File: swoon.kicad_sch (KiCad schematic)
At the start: 130 parts, among them J1 3305-0-15-80-47-27-10-0, J10 3305-0-15-80-47-27-10-0, J11 3305-0-15-80-47-27-10-0, J12 3305-0-15-80-47-27-10-0, J13 3305-0-15-80-47-27-10-0, J14 3305-0-15-80-47-27-10-0, J15 3305-0-15-80-47-27-10-0, J16 3305-0-15-80-47-27-10-0, J17 3305-0-15-80-47-27-10-0, J18 3305-0-15-80-47-27-10-0, J19 3305-0-15-80-47-27-10-0, J2 3305-0-15-80-47-27-10-0, J20 3305-0-15-80-47-27-10-0, J21 3305-0-15-80-47-27-10-0, J22 3305-0-15-80-47-27-10-0, J23 3305-0-15-80-47-27-10-0, J24 3305-0-15-80-47-27-10-0, J25 3305-0-15-80-47-27-10-0, J26 3305-0-15-80-47-27-10-0, J27 3305-0-15-80-47-27-10-0, J28 3305-0-15-80-47-27-10-0, J29 3305-0-15-80-47-27-10-0, J3 3305-0-15-80-47-27-10-0, J30 3305-0-15-80-47-27-10-0, J31 3305-0-15-80-47-27-10-0, J32 3305-0-15-80-47-27-10-0, J33 3305-0-15-80-47-27-10-0, J34 3305-0-15-80-47-27-10-0, J35 3305-0-15-80-47-27-10-0, J36 3305-0-15-80-47-27-10-0, J37 3305-0-15-80-47-27-10-0, J38 3305-0-15-80-47-27-10-0, J39 3305-0-15-80-47-27-10-0, J4 3305-0-15-80-47-27-10-0, J40 3305-0-15-80-47-27-10-0, J41 3305-0-15-80-47-27-10-0, J42 3305-0-15-80-47-27-10-0, J43 3305-0-15-80-47-27-10-0, J44 3305-0-15-80-47-27-10-0, J45 3305-0-15-80-47-27-10-0, J46 3305-0-15-80-47-27-10-0, J47 3305-0-15-80-47-27-10-0, J48 3305-0-15-80-47-27-10-0, J49 3305-0-15-80-47-27-10-0, J5 3305-0-15-80-47-27-10-0, J50 3305-0-15-80-47-27-10-0, J51 3305-0-15-80-47-27-10-0, J52 3305-0-15-80-47-27-10-0, J53 3305-0-15-80-47-27-10-0, J54 3305-0-15-80-47-27-10-0, J55 3305-0-15-80-47-27-10-0, J56 3305-0-15-80-47-27-10-0, J57 3305-0-15-80-47-27-10-0, J58 3305-0-15-80-47-27-10-0, J59 3305-0-15-80-47-27-10-0, J6 3305-0-15-80-47-27-10-0, J60 3305-0-15-80-47-27-10-0, J61 3305-0-15-80-47-27-10-0, J62 3305-0-15-80-47-27-10-0, J63 3305-0-15-80-47-27-10-0, J64 3305-0-15-80-47-27-10-0, J65 3305-0-15-80-47-27-10-0, J66 3305-0-15-80-47-27-10-0, J67 3305-0-15-80-47-27-10-0, J68 3305-0-15-80-47-27-10-0, J69 MF254V-11-07-0743, J7 3305-0-15-80-47-27-10-0, J70 MF254V-11-07-0743, J71 MF254V-11-07-0743, J72 MF254V-11-07-0743, J73 Mill Max 0906-2-15-20-75-14-1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, J74 Mill Max 0906-2-15-20-75-14-1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, J75 JST SM02B-SRSS-TB(LF)(SN), J76 JST SM02B-SRSS-TB(LF)(SN), J8 3305-0-15-80-47-27-10-0, J9 3305-0-15-80-47-27-10-0, SW1 SW_Push, SW10 SW_Push, SW11 SW_Push, SW12 SW_Push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

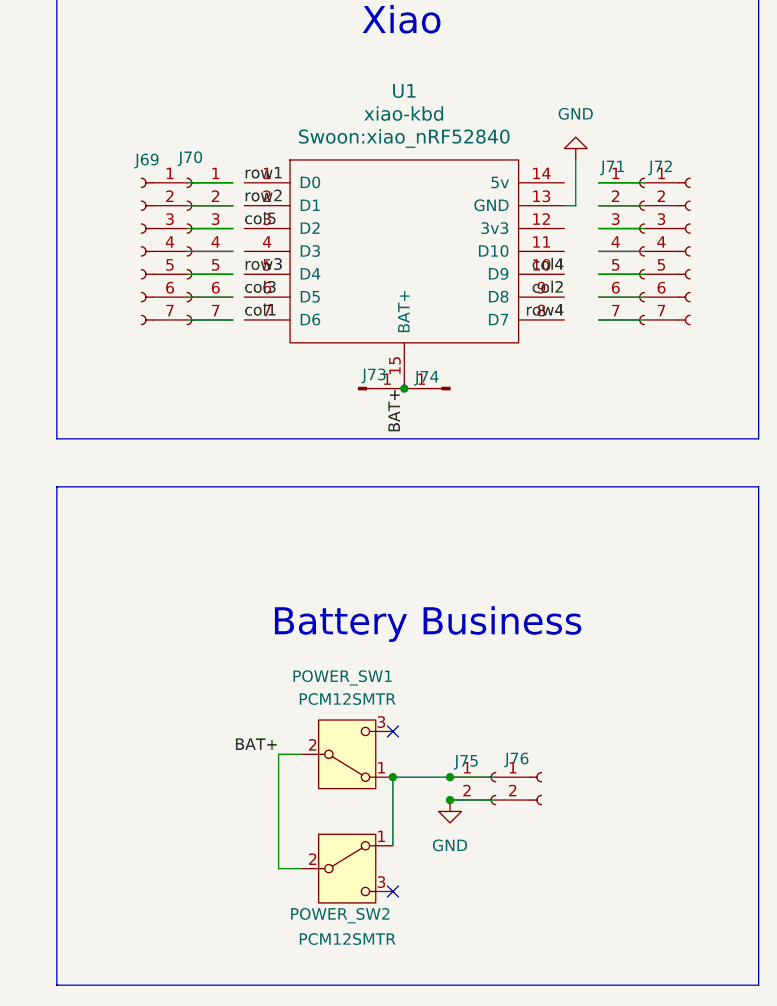
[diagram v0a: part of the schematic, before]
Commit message: position battery terminal & power switch
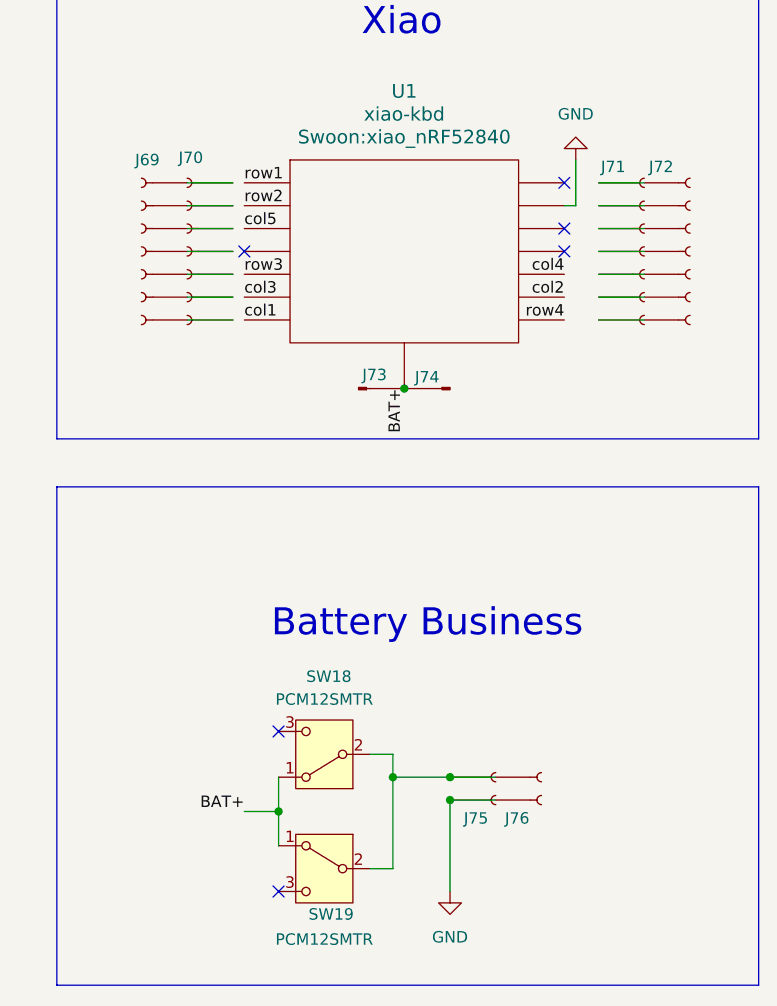
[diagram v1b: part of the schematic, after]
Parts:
- renumbered POWER_SW1 to SW18, POWER_SW2 to SW19
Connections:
- net BAT+: now also SW18.1 (A), SW19.1 (A); no longer SW18.2 (B), SW19.2 (B)
- net GND: now also J75.1 (Pin_1), J76.1 (Pin_1); no longer J75.2 (Pin_2), J76.2 (Pin_2)
- new net: J75.2 (Pin_2), J76.2 (Pin_2), SW18.2 (B), SW19.2 (B)
- no-connect marks 2 -> 6
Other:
- moved on the sheet: SW18, SW19

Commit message: add tenting puck, copper graphic
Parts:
- added H1: Puck_Mounting_Pad, Swoon:Tenting_Puck2, symbol Mechanical:MountingHole_Pad_MP
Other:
- note added: "Mounting Puck"
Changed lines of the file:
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@@
 	)
 	(rectangle
+		(start 24.892 166.37)
+		(end 172.466 192.278)
+		(stroke
+			(width 0)
+			(type default)
+		)
+		(fill
+			(type none)
+		)
+	)
+	(rectangle
 		(start 186.182 32.766)
 		(end 264.16 88.138)
@@
 		)
 	)
+	(text "Mounting Puck\n"
+		(exclude_from_sim no)
+		(at 70.612 178.816 0)
+		(effects
+			(font
+				(size 2.9972 2.9972)
+			)
+		)
+	)
 	(text "Battery Business"
 		(exclude_from_sim no)
@@
 					(unit 1)
 				)
+			)
+		)
+	)
+	(symbol
+		(lib_id "Mechanical:MountingHole_Pad_MP")
+		(at 104.14 179.07 0)
+		(unit 1)
+		(exclude_from_sim yes)
+		(in_bom no)
+		(on_board yes)
+		(dnp no)
+		(fields_autoplaced yes)
+		(property "Reference" "H1"
+			(at 106.68 176.5299 0)
+			(effects
+				(font
+					(size 1.27 1.27)
+				)
+				(justify left)
+			)
+		)
+		(property "Value" "Puck_Mounting_Pad"
+			(at 106.68 179.0699 0)
+			(effects
+				(font
+					(size 1.27 1.27)
+				)
+				(justify left)
+			)
+		)
+		(property "Footprint" "Swoon:Tenting_Puck2"
+			(at 104.14 179.07 0)
+			(effects
+				(font
+					(size 1.27 1.27)
+				)
+				(hide yes)
+			)
+		)
+		(property "Datasheet" "~"
+			(at 104.14 179.07 0)
+			(effects
+				(font
+					(size 1.27 1.27)
+				)
+				(hide yes)
+			)
+		)
+		(property "Description" "Mounting Hole with connection as pad named MP"
+			(at 104.14 179.07 0)
+			(effects
+				(font
+					(size 1.27 1.27)
+				)
+				(hide yes)
+			)
+		)
+		(pin "MP"
+		)
+		(instances
+			(project ""
+				(path "/1418ad6a-8a4d-429d-b07e-469b1ffa21a0"
+					(reference "H1")
+					(unit 1)
+				)

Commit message: add kicad action
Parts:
- D1, D10, D11, D12, D13, D14, D15, D16, D17, D18, D19, D2, D20, D21, D22, D23, D24, D25, D26, D27, D28, D29, D3, D30, D31, D32, D33, D34, D4, D5, D6, D7, D8, D9: footprint Diode_SMD:D_0805_2012Metric -> Swoon:D_0805_2012Metric
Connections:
- no-connect marks 6 -> 7
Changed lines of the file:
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@@
 	)
 	(no_connect
+		(at 104.14 181.61)
+	)
+	(no_connect
 		(at 210.82 120.65)
 	)
@@
 			)
 		)
-		(property "Footprint" "Diode_SMD:D_0805_2012Metric"
+		(property "Footprint" "Swoon:D_0805_2012Metric"
 			(at 142.24 82.55 0)
 			(effects
@@
 			)
 		)
-		(property "Footprint" "Diode_SMD:D_0805_2012Metric"
+		(property "Footprint" "Swoon:D_0805_2012Metric"
 			(at 77.47 123.19 0)
 			(effects
@@
 			)
 		)
-		(property "Footprint" "Diode_SMD:D_0805_2012Metric"
+		(property "Footprint" "Swoon:D_0805_2012Metric"
 			(at 97.79 82.55 0)
 			(effects
@@
 			)
 		)
-		(property "Footprint" "Diode_SMD:D_0805_2012Metric"
+		(property "Footprint" "Swoon:D_0805_2012Metric"
 			(at 142.24 102.87 0)
 			(effects
@@
 			)
 		)
-		(property "Footprint" "Diode_SMD:D_0805_2012Metric"
+		(property "Footprint" "Swoon:D_0805_2012Metric"
 			(at 57.15 62.23 0)
 			(effects
@@
 			)
 		)
-		(property "Footprint" "Diode_SMD:D_0805_2012Metric"
+		(property "Footprint" "Swoon:D_0805_2012Metric"
 			(at 81.28 102.87 0)
 			(effects
@@
 			)
 		)
-		(property "Footprint" "Diode_SMD:D_0805_2012Metric"
+		(property "Footprint" "Swoon:D_0805_2012Metric"
 			(at 60.96 123.19 0)
 			(effects
@@
 			)
 		)
-		(property "Footprint" "Diode_SMD:D_0805_2012Metric"
+		(property "Footprint" "Swoon:D_0805_2012Metric"
 			(at 97.79 62.23 0)
 			(effects
@@
 			)
 		)
-		(property "Footprint" "Diode_SMD:D_0805_2012Metric"
+		(property "Footprint" "Swoon:D_0805_2012Metric"
 			(at 81.28 123.19 0)
 			(effects
@@
 			)
 		)
-		(property "Footprint" "Diode_SMD:D_0805_2012Metric"
+		(property "Footprint" "Swoon:D_0805_2012Metric"
 			(at 77.47 82.55 0)
 			(effects
@@
 			)
 		)
-		(property "Footprint" "Diode_SMD:D_0805_2012Metric"
+		(property "Footprint" "Swoon:D_0805_2012Metric"
 			(at 60.96 62.23 0)
 			(effects
@@
 			)
 		)
-		(property "Footprint" "Diode_SMD:D_0805_2012Metric"
+		(property "Footprint" "Swoon:D_0805_2012Metric"
 			(at 77.47 62.23 0)
 			(effects
@@
 			)
 		)
-		(property "Footprint" "Diode_SMD:D_0805_2012Metric"
+		(property "Footprint" "Swoon:D_0805_2012Metric"
 			(at 57.15 102.87 0)
 			(effects
@@
 			)
 		)
+		(property "LCSC" ""
+			(at 224.79 67.31 0)
+			(effects
+				(font
+					(size 1.27 1.27)
+				)
+				(hide yes)
+			)
+		)
 		(pin "11"
 		)
@@
 			)
 		)
-		(property "Footprint" "Diode_SMD:D_0805_2012Metric"
+		(property "Footprint" "Swoon:D_0805_2012Metric"
 			(at 101.6 82.55 0)
 			(effects
@@
 			)
 		)
-		(property "Footprint" "Diode_SMD:D_0805_2012Metric"
+		(property "Footprint" "Swoon:D_0805_2012Metric"
 			(at 138.43 62.23 0)
 			(effects
@@
 			)
 		)
-		(property "Footprint" "Diode_SMD:D_0805_2012Metric"
+		(property "Footprint" "Swoon:D_0805_2012Metric"
 			(at 101.6 62.23 0)
 			(effects
@@
 			)
 		)
-		(property "Footprint" "Diode_SMD:D_0805_2012Metric"
+		(property "Footprint" "Swoon:D_0805_2012Metric"
 			(at 121.92 82.55 0)
 			(effects
@@
 			)
 		)
-		(property "Footprint" "Diode_SMD:D_0805_2012Metric"
+		(property "Footprint" "Swoon:D_0805_2012Metric"
 			(at 60.96 102.87 0)
 			(effects
@@
 			)
 		)
-		(property "Footprint" "Diode_SMD:D_0805_2012Metric"
+		(property "Footprint" "Swoon:D_0805_2012Metric"
 			(at 121.92 62.23 0)
 			(effects
@@
 			)
 		)
-		(property "Footprint" "Diode_SMD:D_0805_2012Metric"
+		(property "Footprint" "Swoon:D_0805_2012Metric"
 			(at 101.6 102.87 0)
 			(effects
@@
 			)
 		)
-		(property "Footprint" "Diode_SMD:D_0805_2012Metric"
+		(property "Footprint" "Swoon:D_0805_2012Metric"
 			(at 118.11 62.23 0)
 			(effects
@@
 			)
 		)
-		(property "Footprint" "Diode_SMD:D_0805_2012Metric"
+		(property "Footprint" "Swoon:D_0805_2012Metric"
 			(at 60.96 82.55 0)
 			(effects
@@
 			)
 		)
-		(property "Footprint" "Diode_SMD:D_0805_2012Metric"
+		(property "Footprint" "Swoon:D_0805_2012Metric"
 			(at 77.47 102.87 0)
 			(effects
@@
 			)
 		)
-		(property "Footprint" "Diode_SMD:D_0805_2012Metric"
+		(property "Footprint" "Swoon:D_0805_2012Metric"
 			(at 81.28 82.55 0)
 			(effects
@@
 			)
 		)
-		(property "Footprint" "Diode_SMD:D_0805_2012Metric"
+		(property "Footprint" "Swoon:D_0805_2012Metric"
 			(at 81.28 62.23 0)
 			(effects
@@
 			)
 		)
-		(property "Footprint" "Diode_SMD:D_0805_2012Metric"
+		(property "Footprint" "Swoon:D_0805_2012Metric"
 			(at 57.15 123.19 0)
 			(effects
@@
 			)
 		)
-		(property "Footprint" "Diode_SMD:D_0805_2012Metric"
+		(property "Footprint" "Swoon:D_0805_2012Metric"
 			(at 57.15 82.55 0)
 			(effects
@@
 			)
 		)
-		(property "Footprint" "Diode_SMD:D_0805_2012Metric"
+		(property "Footprint" "Swoon:D_0805_2012Metric"
 			(at 138.43 82.55 0)
 			(effects
@@
 			)
 		)
-		(property "Footprint" "Diode_SMD:D_0805_2012Metric"
+		(property "Footprint" "Swoon:D_0805_2012Metric"
 			(at 97.79 102.87 0)
 			(effects
@@
 			)
 		)
-		(property "Footprint" "Diode_SMD:D_0805_2012Metric"
+		(property "Footprint" "Swoon:D_0805_2012Metric"
 			(at 118.11 102.87 0)
 			(effects
@@
 			)
 		)
-		(property "Footprint" "Diode_SMD:D_0805_2012Metric"
+		(property "Footprint" "Swoon:D_0805_2012Metric"
 			(at 121.92 102.87 0)
 			(effects
@@
 			)
 		)
-		(property "Footprint" "Diode_SMD:D_0805_2012Metric"
+		(property "Footprint" "Swoon:D_0805_2012Metric"
 			(at 142.24 62.23 0)
 			(effects
@@
 			)
 		)
-		(property "Footprint" "Diode_SMD:D_0805_2012Metric"
+		(property "Footprint" "Swoon:D_0805_2012Metric"
 			(at 118.11 82.55 0)
 			(effects
@@
 			)
 		)
-		(property "Footprint" "Diode_SMD:D_0805_2012Metric"
+		(property "Footprint" "Swoon:D_0805_2012Metric"
 			(at 138.43 102.87 0)
 			(effects

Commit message: add kibot file
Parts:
- removed J75, J76: JST SM02B-SRSS-TB(LF)(SN), Swoon:JST_SH_SM02B-SRSS-TB_1x02-1MP_P1.00mm_Horizontal, symbol Connector:Conn_01x02_Socket
- removed SW18, SW19: PCM12SMTR, Swoon:SW_PCM12SMTR, symbol Switch:SW_SPDT
- added SW18, SW19: MST22D18G2 125, Swoon:SW-SMD_MST22D18G2, symbol Swoon:MST22D18G2125
- added U2, U3: MY-LR44-02, Swoon:BAT-SMD_MY-LR44-02, symbol Swoon:MY-LR44-02
- D1, D10, D11, D12, D13, D14, D15, D16, D17, D18, D19, D2, D20, D21, D22, D23, D24, D25, D26, D27, D28, D29, D3, D30, D31, D32, D33, D34, D4, D5, D6, D7, D8, D9: value CD4148WSP-C109001 -> CD4148W; footprint Swoon:D_0805_2012Metric -> Diode_SMD:D_0805_2012Metric; LCSC (none) -> C109001
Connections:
- net BAT+: now also SW18.1, SW18.2, SW18.4, SW18.5, SW19.1, SW19.2, SW19.4, SW19.5
- net GND: now also U2.2, U3.2
- new net: SW18.3, SW18.6, SW19.3, SW19.6, U2.1, U3.1
- no-connect marks 7 -> 5

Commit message: add variants
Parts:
- added TP1, TP10, TP11, TP12, TP13, TP14, TP15, TP16, TP17, TP18, TP19, TP2, TP20, TP3, TP4, TP5, TP6, TP7, TP8, TP9: TestPoint_Small, TestPoint:TestPoint_Pad_1.0x1.0mm, symbol Connector:TestPoint_Small
- D1, D11, D13, D15, D17, D19, D21, D23, D25, D27, D29, D3, D31, D33, D5, D7, D9: value CD4148W -> CD4148WS; footprint Diode_SMD:D_0805_2012Metric -> Swoon:D_0805_2012Metric; Config (none) -> +left,+flip; LCSC C109001 -> C38587762
- D10, D12, D14, D16, D18, D2, D20, D22, D24, D26, D28, D30, D32, D34, D4, D6, D8: value CD4148W -> CD4148WS; footprint Diode_SMD:D_0805_2012Metric -> Swoon:D_0805_2012Metric; Config (none) -> +right,+flip; LCSC C109001 -> C38587762
- J1, J10, J13, J14, J17, J18, J2, J21, J22, J25, J26, J29, J30, J33, J34, J37, J38, J41, J42, J45, J46, J49, J5, J50, J53, J54, J57, J58, J6, J61, J62, J65, J66, J9: Config (none) -> +left,+flip; LCSC (none) -> C17370797
- J11, J12, J15, J16, J19, J20, J23, J24, J27, J28, J3, J31, J32, J35, J36, J39, J4, J40, J43, J44, J47, J48, J51, J52, J55, J56, J59, J60, J63, J64, J67, J68, J7, J8: Config (none) -> +right,+flip; LCSC (none) -> C17370797
- J69, J71: value MF254V-11-07-0743 -> 310-13-107-41-001000; Config (none) -> +left,+flip; LCSC (none) -> C5504401
- J70, J72: value MF254V-11-07-0743 -> 310-13-107-41-001000; Config (none) -> +right,+flip; LCSC (none) -> C5504401
- J73: Config (none) -> +left,+flip; LCSC (none) -> C5261048
- J74: Config (none) -> +right,+flip; LCSC (none) -> C5261048
- SW18: Config (none) -> +left,+flip; LCSC (none) -> C2906280; LCSC Part C2906280 -> (none)
- SW19: Config (none) -> +right,+flip; LCSC (none) -> C2906280; LCSC Part C2906280 -> (none)
- U1: footprint Swoon:xiao_nRF52840 -> Swoon:xiao_nRF52840_extra; symbol Swoon:xiao_nRF52840 -> Swoon:xiao_nRF52840_extra; now in the parts list
- U2: Config (none) -> +left,+flip; LCSC (none) -> C2902345; LCSC Part C2902345 -> (none)
- U3: Config (none) -> +right,+flip; LCSC (none) -> C2902345; LCSC Part C2902345 -> (none)
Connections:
- net BAT+: now also U2.2, U3.4; no longer SW18.1, SW18.2, SW18.4, SW18.5, SW19.1, SW19.2, SW19.4, SW19.5
- net GND: now also SW18.1, SW18.2, SW18.4, SW18.5, SW19.1, SW19.2, SW19.4, SW19.5; no longer U2.2, U3.2
- net col4: now also U1.5 (D4); no longer U1.10 (D9)
- net row3: now also U1.10 (D9); no longer U1.5 (D4)
- net at J69.1 (Pin_1), J70.1 (Pin_1): now also U1.16 (hole), TP1.1, TP2.1
- net at J69.2 (Pin_2), J70.2 (Pin_2): now also U1.17 (hole), TP3.1, TP4.1
- net at J69.3 (Pin_3), J70.3 (Pin_3): now also U1.18 (hole), TP5.1, TP6.1
- net at J69.4 (Pin_4), J70.4 (Pin_4): now also U1.19 (hole)
- net at J69.5 (Pin_5), J70.5 (Pin_5): now also U1.20 (hole), TP7.1, TP8.1
- net at J69.6 (Pin_6), J70.6 (Pin_6): now also U1.21 (hole), TP10.1, TP9.1
- net at J69.7 (Pin_7), J70.7 (Pin_7): now also U1.22 (hole), TP11.1, TP12.1
- net at J71.1 (Pin_1), J72.1 (Pin_1): now also U1.29 (hole)
- net at J71.2 (Pin_2), J72.2 (Pin_2): now also U1.28 (hole), TP19.1, TP20.1
- net at J71.3 (Pin_3), J72.3 (Pin_3): now also U1.27 (hole)
- net at J71.4 (Pin_4), J72.4 (Pin_4): now also U1.26 (hole)
- net at J71.5 (Pin_5), J72.5 (Pin_5): now also U1.25 (hole), TP13.1, TP14.1
- net at J71.6 (Pin_6), J72.6 (Pin_6): now also U1.24 (hole), TP15.1, TP16.1
- net at J71.7 (Pin_7), J72.7 (Pin_7): now also U1.23 (hole), TP17.1, TP18.1
- new net: SW18.3, U2.1
- new net: SW19.6, U3.1
- now unconnected: SW18.6, SW19.3
- no-connect marks 5 -> 8
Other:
- company: broomlabs -> Octule
- title: Sweep V2 -> Swoon
- moved on the sheet: J69, J70, J71, J72, SW18, SW19

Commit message: add rotataed variant
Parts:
- J73, J74: LCSC C5261048 -> C5261048
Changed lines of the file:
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@@
 			)
 		)
-		(property "LCSC" " C5261048"
+		(property "LCSC" "C5261048"
 			(at 229.87 82.55 0)
 			(effects
@@
 			)
 		)
-		(property "LCSC" " C5261048"
+		(property "LCSC" "C5261048"
 			(at 219.71 82.55 0)
 			(effects

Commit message: add mpn field
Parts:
- D1, D10, D11, D12, D13, D14, D15, D16, D17, D18, D19, D2, D20, D21, D22, D23, D24, D25, D26, D27, D28, D29, D3, D30, D31, D32, D33, D34, D4, D5, D6, D7, D8, D9: MPN (none) -> CD4148WS(0805C)
- J1, J10, J11, J12, J13, J14, J15, J16, J17, J18, J19, J2, J20, J21, J22, J23, J24, J25, J26, J27, J28, J29, J3, J30, J31, J32, J33, J34, J35, J36, J37, J38, J39, J4, J40, J41, J42, J43, J44, J45, J46, J47, J48, J49, J5, J50, J51, J52, J53, J54, J55, J56, J57, J58, J59, J6, J60, J61, J62, J63, J64, J65, J66, J67, J68, J7, J8, J9: MPN (none) -> 3305-0-15-80-47-27-10-0
- J69, J70, J71, J72: MPN (none) -> 310-13-107-41-001000
- J73, J74: MPN (none) -> 0906-2-15-20-75-14-11-0
- SW18, SW19: MPN (none) -> MST22D18G2 125
- U2, U3: MPN (none) -> MY-LR44-02

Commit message: fix mp errors
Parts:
- H1: symbol Mechanical:MountingHole_Pad_MP -> Connector_Generic_MountingPin:Conn_02x02_Counter_Clockwise_MountingPin; now in the parts list
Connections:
- no-connect marks 8 -> 12
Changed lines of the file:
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@@
 	)
 	(no_connect
+		(at 102.87 180.34)
+	)
+	(no_connect
 		(at 245.11 115.57)
 	)
@@
 	)
 	(no_connect
+		(at 90.17 180.34)
+	)
+	(no_connect
 		(at 245.11 137.16)
 	)
@@
 	)
 	(no_connect
+		(at 102.87 182.88)
+	)
+	(no_connect
 		(at 242.57 59.69)
 	)
 	(no_connect
+		(at 90.17 182.88)
+	)
+	(no_connect
 		(at 201.93 124.46)
 	)
@@
 	)
 	(symbol
-		(lib_id "Mechanical:MountingHole_Pad_MP")
-		(at 104.14 179.07 0)
+		(lib_id "Connector_Generic_MountingPin:Conn_02x02_Counter_Clockwise_MountingPin")
+		(at 95.25 180.34 0)
 		(unit 1)
-		(exclude_from_sim yes)
-		(in_bom no)
+		(exclude_from_sim no)
+		(in_bom yes)
 		(on_board yes)
 		(dnp no)
 		(fields_autoplaced yes)
 		(property "Reference" "H1"
-			(at 106.68 176.5299 0)
+			(at 96.52 173.99 0)
 			(effects
 				(font
 					(size 1.27 1.27)
 				)
-				(justify left)
 			)
 		)
 		(property "Value" "Puck_Mounting_Pad"
-			(at 106.68 179.0699 0)
+			(at 96.52 176.53 0)
 			(effects
 				(font
 					(size 1.27 1.27)
 				)
-				(justify left)
 			)
 		)
 		(property "Footprint" "Swoon:Tenting_Puck2"
-			(at 104.14 179.07 0)
+			(at 95.25 180.34 0)
 			(effects
 				(font
@@
 		)
 		(property "Datasheet" "~"
-			(at 104.14 179.07 0)
+			(at 95.25 180.34 0)
 			(effects
 				(font
@@
 			)
 		)
-		(property "Description" "Mounting Hole with connection as pad named MP"
-			(at 104.14 179.07 0)
+		(property "Description" "Generic connectable mounting pin connector, double row, 02x02, counter clockwise pin numbering scheme (similar to DIP package numbering), script generated (kicad-library-utils/schlib/autogen/connector/)"
+			(at 95.25 180.34 0)
 			(effects
 				(font
@@
 		)
 		(property "Config" ""
-			(at 104.14 179.07 0)
+			(at 95.25 180.34 0)
 			(effects
 				(font
@@
 		)
 		(property "MPN" ""
-			(at 104.14 179.07 0)
+			(at 95.25 180.34 0)
 			(effects
 				(font
@@
 			)
 		)
-		(pin "MP"
+		(pin "1"
+		)
+		(pin "2"
+		)
+		(pin "3"
+		)
+		(pin "4"
 		)
 		(instances
